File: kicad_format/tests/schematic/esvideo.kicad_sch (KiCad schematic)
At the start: 29 parts, among them U8 BT253, U9 BT473

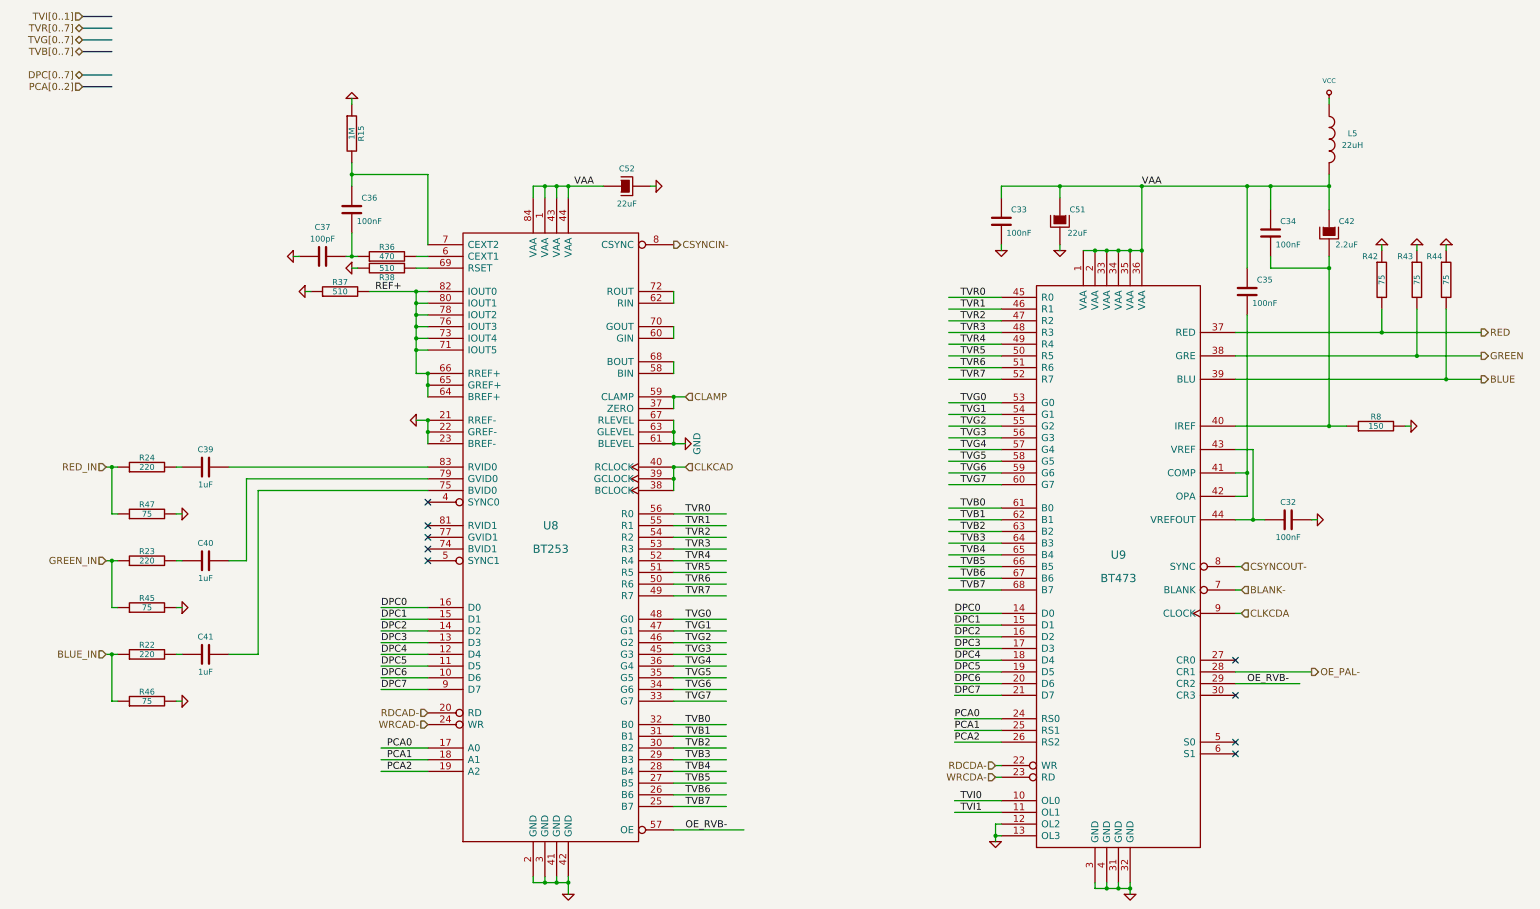
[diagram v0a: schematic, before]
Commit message: Add serialization context and support most modern kicad file idiosyncrasies
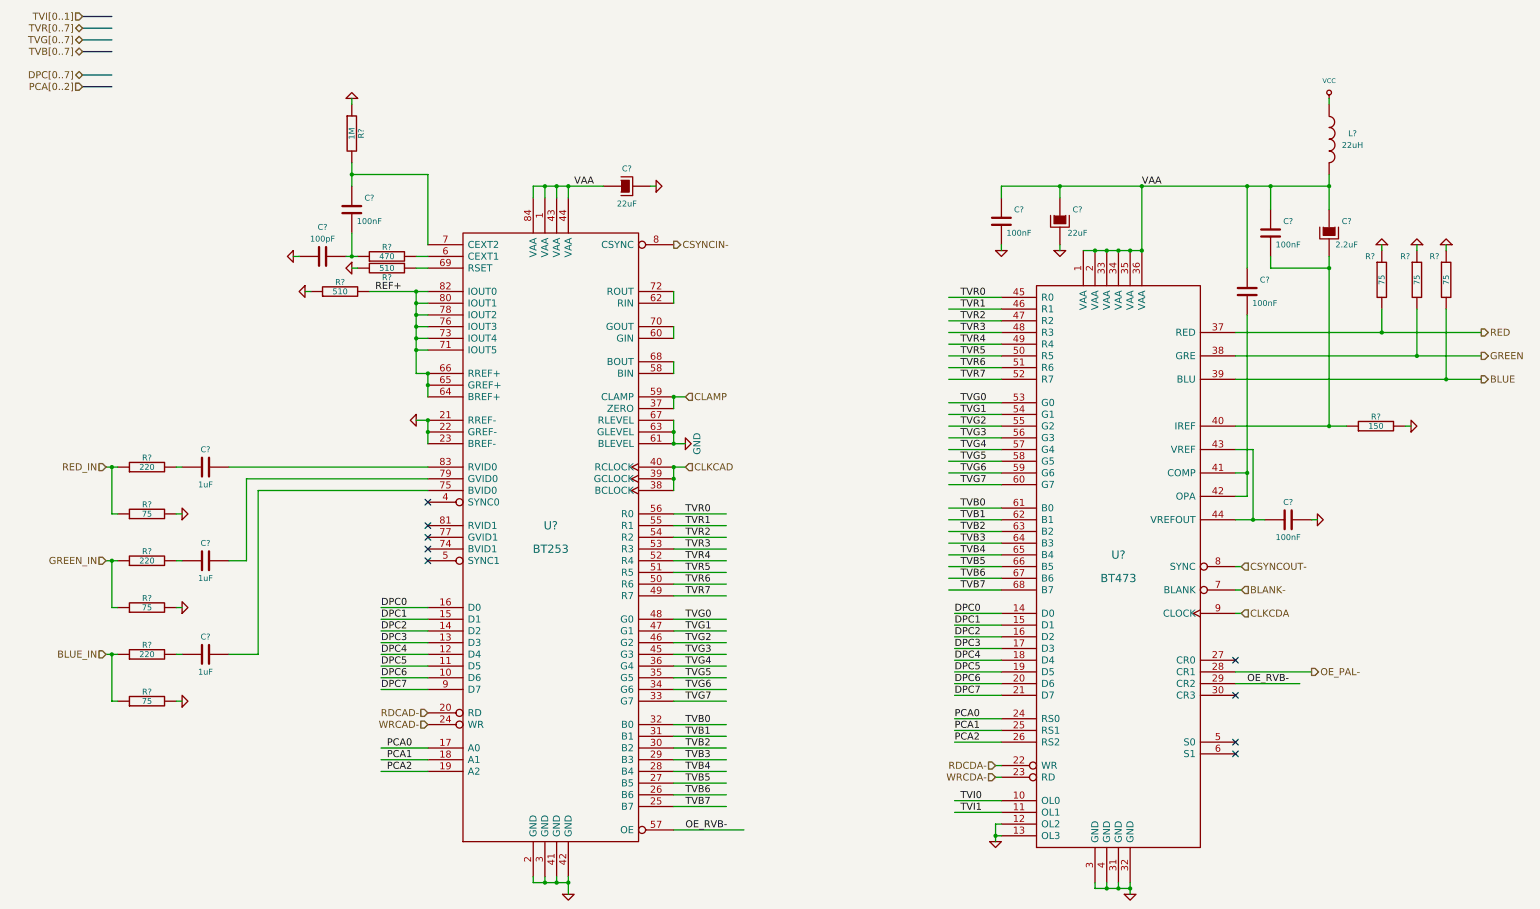
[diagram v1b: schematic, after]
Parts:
- renumbered C51 to C?, C32 to C?, C36 to C?, C40 to C?, C52 to C?, C34 to C?, C37 to C?, C33 to C?, C39 to C?, C41 to C?, C42 to C?, C35 to C?, L5 to L?, R37 to R?, R36 to R?, R23 to R?, R44 to R?, R45 to R?, R46 to R?, R22 to R?, R38 to R?, R47 to R?, R24 to R?, R43 to R?, R42 to R?, R8 to R?, R15 to R?, U8 to U?, U9 to U?
